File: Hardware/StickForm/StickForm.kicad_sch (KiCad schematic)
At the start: 62 parts, among them J1 48037-0001, J2 JTAG, J3 SWD, U1 SRV05-4, U10 SRV05-4, U11 SRV05-4, U2 STM32L432KBU6, U3 ME6211A33M3G-N, U4 AD8531ARTZ, U5 74AVCH2T45DC, U6 74LVC2G125, U7 74LVC2G125, U8 74LVC2G125, U9 74LVC2G125, Y1 32768 7pF

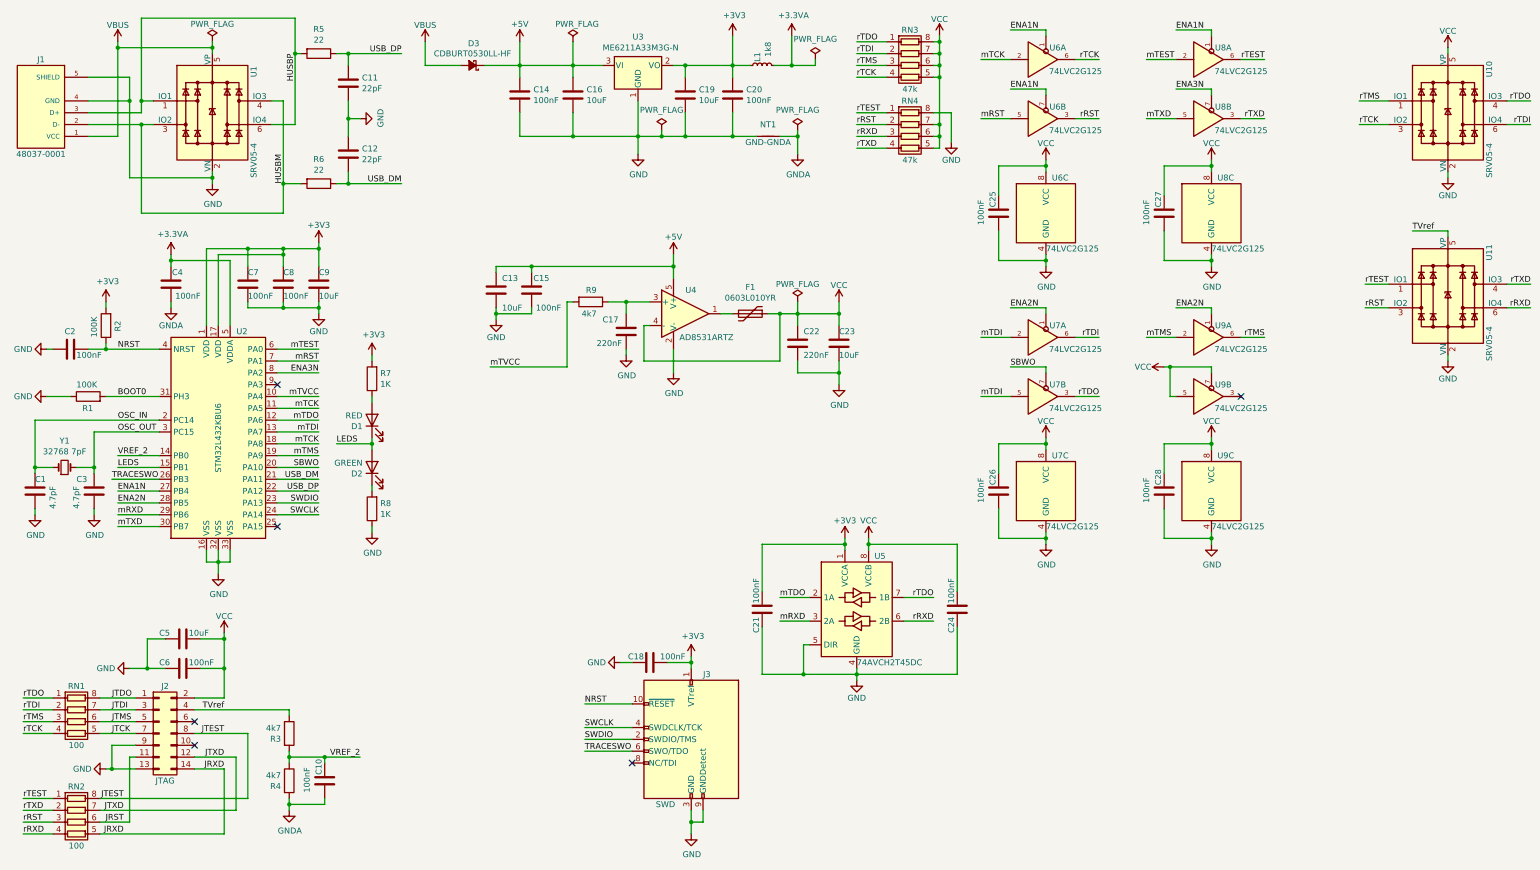
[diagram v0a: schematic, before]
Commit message: Updated Stick Form Glossy MSP430 device
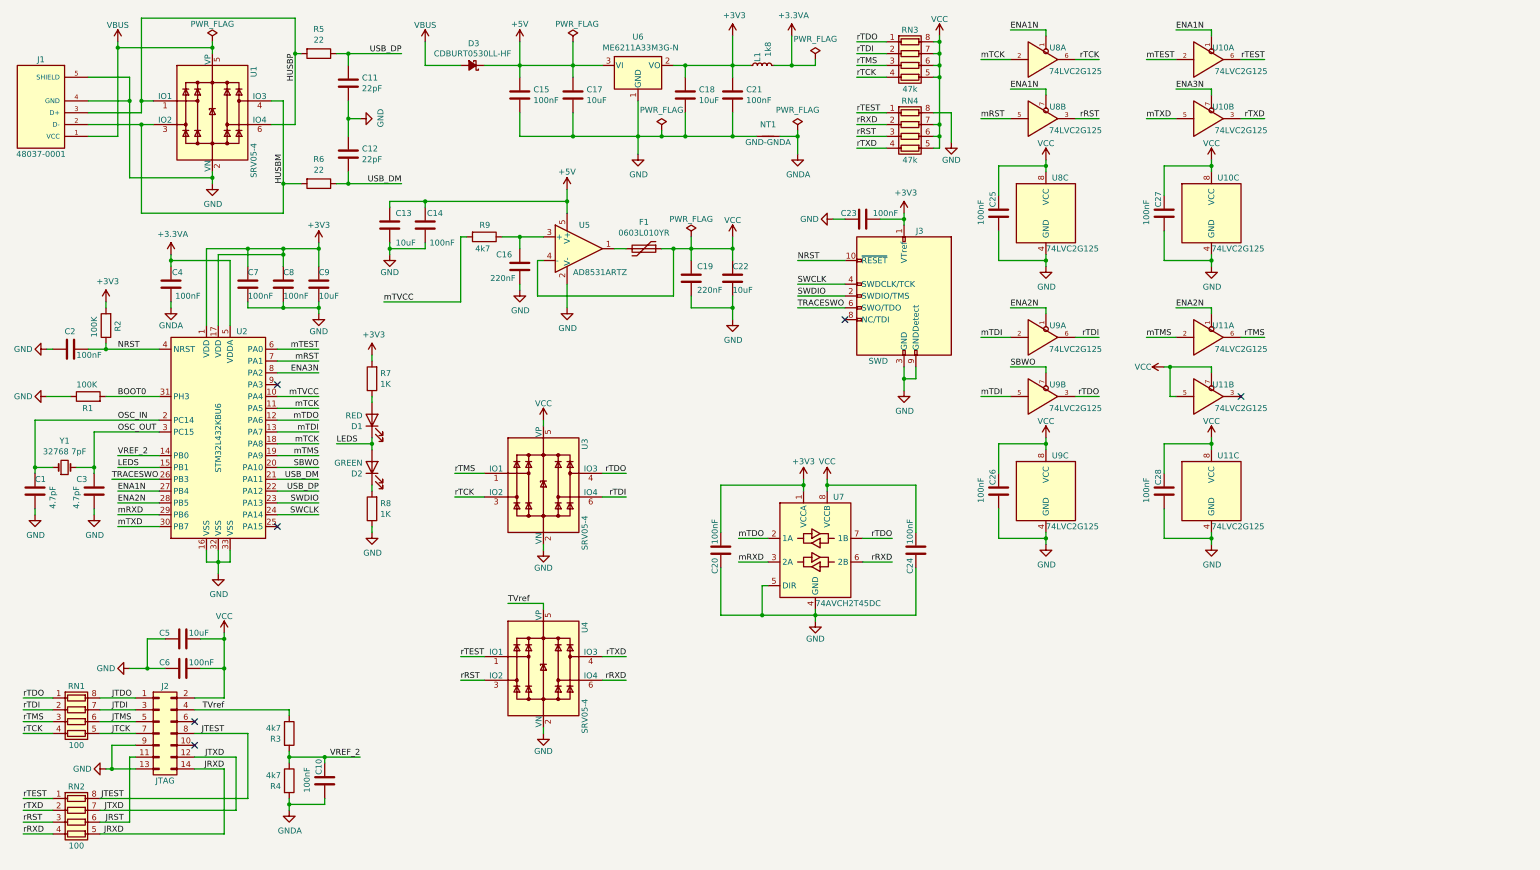
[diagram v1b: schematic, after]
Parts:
- renumbered C15 to C14, C14 to C15, C17 to C16, C16 to C17, C19 to C18, C22 to C19, C21 to C20, C20 to C21, C23 to C22, C18 to C23, U8 to U10, U9 to U11, U10 to U3, U11 to U4, U4 to U5, U3 to U6, U5 to U7, U6 to U8, U7 to U9
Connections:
- net rRST: now also RN4.3 (R3.1); no longer RN4.2 (R2.1)
- net rRXD: now also RN4.2 (R2.1); no longer RN4.3 (R3.1)
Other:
- title: Black Magic Probe MSP430 Edition - Stick II -> Glossy MSP430 Stick Version
- moved on the sheet: C13, C14, C16, C19, C20, C22, C23, C24, F1, J3, R9, U3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

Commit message: Updated schematics for StickForm (WIP)
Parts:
- removed R2: 100K, Resistor_SMD:R_0402_1005Metric_Pad0.72x0.64mm_HandSolder, symbol Device:R
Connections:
- net HUSBM: no longer U1.3 (IO2)
- net HUSBP: no longer U1.1 (IO1)
- no-connect marks 6 -> 8
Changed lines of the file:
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@@
   (junction (at 78.74 64.77) (diameter 0) (color 0 0 0 0)
   )
-  (junction (at 40.64 38.1) (diameter 0) (color 0 0 0 0)
-  )
   (junction (at 133.35 40.64) (diameter 0) (color 0 0 0 0)
   )
@@
   (junction (at 212.09 25.4) (diameter 0) (color 0 0 0 0)
   )
-  (junction (at 40.64 33.02) (diameter 0) (color 0 0 0 0)
-  )
   (junction (at 132.08 54.61) (diameter 0) (color 0 0 0 0)
   )
@@
   (junction (at 182.88 115.57) (diameter 0) (color 0 0 0 0)
   )
-  (junction (at 33.02 86.36) (diameter 0) (color 0 0 0 0)
-  )
   (junction (at 63.5 64.77) (diameter 0) (color 0 0 0 0)
   )
@@
   (no_connect (at 69.85 124.46))
   (no_connect (at 191.77 80.01))
+  (no_connect (at 43.18 38.1))
+  (no_connect (at 43.18 33.02))
   (no_connect (at 69.85 93.98))
   (no_connect (at 276.86 96.52))
@@
     (stroke (width 0) (type default) (color 0 0 0 0))
   )
-  (wire (pts (xy 40.64 35.56) (xy 40.64 33.02))
-    (stroke (width 0) (type default) (color 0 0 0 0))
-  )
   (wire (pts (xy 194.31 25.4) (xy 200.66 25.4))
     (stroke (width 0) (type default) (color 0 0 0 0))
@@
     (stroke (width 0) (type default) (color 0 0 0 0))
   )
-  (wire (pts (xy 33.02 76.2) (xy 33.02 77.47))
-    (stroke (width 0) (type default) (color 0 0 0 0))
-  )
   (wire (pts (xy 26.67 111.76) (xy 30.48 111.76))
     (stroke (width 0) (type default) (color 0 0 0 0))
@@
     (stroke (width 0) (type default) (color 0 0 0 0))
   )
-  (wire (pts (xy 33.02 86.36) (xy 44.45 86.36))
-    (stroke (width 0) (type default) (color 0 0 0 0))
-  )
   (wire (pts (xy 78.74 78.74) (xy 78.74 77.47))
     (stroke (width 0) (type default) (color 0 0 0 0))
@@
     (stroke (width 0) (type default) (color 0 0 0 0))
   )
-  (wire (pts (xy 40.64 33.02) (xy 40.64 15.24))
+  (wire (pts (xy 40.64 15.24) (xy 40.64 35.56))
     (stroke (width 0) (type default) (color 0 0 0 0))
   )
@@
     (stroke (width 0) (type default) (color 0 0 0 0))
   )
-  (wire (pts (xy 29.21 86.36) (xy 33.02 86.36))
+  (wire (pts (xy 29.21 86.36) (xy 44.45 86.36))
     (stroke (width 0) (type default) (color 0 0 0 0))
   )
@@
     (stroke (width 0) (type default) (color 0 0 0 0))
   )
-  (wire (pts (xy 40.64 33.02) (xy 43.18 33.02))
-    (stroke (width 0) (type default) (color 0 0 0 0))
-  )
   (wire (pts (xy 57.15 81.28) (xy 57.15 66.04))
     (stroke (width 0) (type default) (color 0 0 0 0))
@@
     (stroke (width 0) (type default) (color 0 0 0 0))
   )
-  (wire (pts (xy 33.02 85.09) (xy 33.02 86.36))
-    (stroke (width 0) (type default) (color 0 0 0 0))
-  )
   (wire (pts (xy 167.64 64.77) (xy 158.75 64.77))
     (stroke (width 0) (type default) (color 0 0 0 0))
@@
     (stroke (width 0) (type default) (color 0 0 0 0))
   )
-  (wire (pts (xy 40.64 38.1) (xy 43.18 38.1))
-    (stroke (width 0) (type default) (color 0 0 0 0))
-  )
   (wire (pts (xy 241.3 83.82) (xy 246.38 83.82))
     (stroke (width 0) (type default) (color 0 0 0 0))
@@
     (pin "1")
   )
-  (symbol (lib_id "power:+3V3") (at 33.02 76.2 0) (unit 1)
-    (in_bom yes) (on_board yes)
-    (property "Reference" "#PWR05" (id 0) (at 33.02 80.01 0)
-      (effects (font (size 1.27 1.27)) hide)
-    )
-    (property "Value" "+3V3" (id 1) (at 33.401 71.8058 0))
-    (property "Footprint" "" (id 2) (at 33.02 76.2 0)
-      (effects (font (size 1.27 1.27)) hide)
-    )
-    (property "Datasheet" "" (id 3) (at 33.02 76.2 0)
-      (effects (font (size 1.27 1.27)) hide)
-    )
-    (pin "1")
-  )
   (symbol (lib_id "Device:C") (at 25.4 86.36 270) (unit 1)
     (in_bom yes) (on_board yes)
@@
     (pin "2")
   )
-  (symbol (lib_id "Device:R") (at 33.02 81.28 180) (unit 1)
-    (in_bom yes) (on_board yes)
-    (property "Reference" "R2" (id 0) (at 35.56 82.55 90)
-      (effects (font (size 1.27 1.27)) (justify right))
-    )
-    (property "Value" "100K" (id 1) (at 30.48 83.82 90)
-      (effects (font (size 1.27 1.27)) (justify right))
-    )
-    (property "Footprint" "Resistor_SMD:R_0402_1005Metric_Pad0.72x0.64mm_HandSolder" (id 2) (at 34.798 81.28 90)
-      (effects (font (size 1.27 1.27)) hide)
-    )
-    (property "Datasheet" "~" (id 3) (at 33.02 81.28 0)
-      (effects (font (size 1.27 1.27)) hide)
-    )
-    (property "LCSC" "C25741" (id 4) (at 33.02 81.28 90)
-      (effects (font (size 1.27 1.27)) hide)
-    )
-    (property "Descr" "100kΩ ±1% 1/16W ±100ppm/℃ 0402 Chip Resistor - Surface Mount RoHS" (id 5) (at 22.86 78.74 0)
-      (effects (font (size 1.27 1.27)) hide)
-    )
-    (pin "1")
-    (pin "2")
-  )
   (symbol (lib_id "Device:R") (at 78.74 50.8 270) (unit 1)
     (in_bom yes) (on_board yes)
@@
       (reference "#PWR04") (unit 1) (value "GND") (footprint "")
     )
-    (path "/00000000-0000-0000-0000-000061002470"
-      (reference "#PWR05") (unit 1) (value "+3V3") (footprint "")
-    )
     (path "/00000000-0000-0000-0000-000060c1316b"
       (reference "#PWR06") (unit 1) (value "GND") (footprint "")
@@
       (reference "R1") (unit 1) (value "100K") (footprint "Resistor_SMD:R_0402_1005Metric_Pad0.72x0.64mm_HandSolder")
     )
-    (path "/00000000-0000-0000-0000-00006102ed2f"
-      (reference "R2") (unit 1) (value "100K") (footprint "Resistor_SMD:R_0402_1005Metric_Pad0.72x0.64mm_HandSolder")
-    )
     (path "/00000000-0000-0000-0000-00006102042d"
